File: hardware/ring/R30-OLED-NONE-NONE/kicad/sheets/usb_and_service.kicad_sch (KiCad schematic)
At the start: 4 parts, among them J1 USB4215-class 16P TH stakes

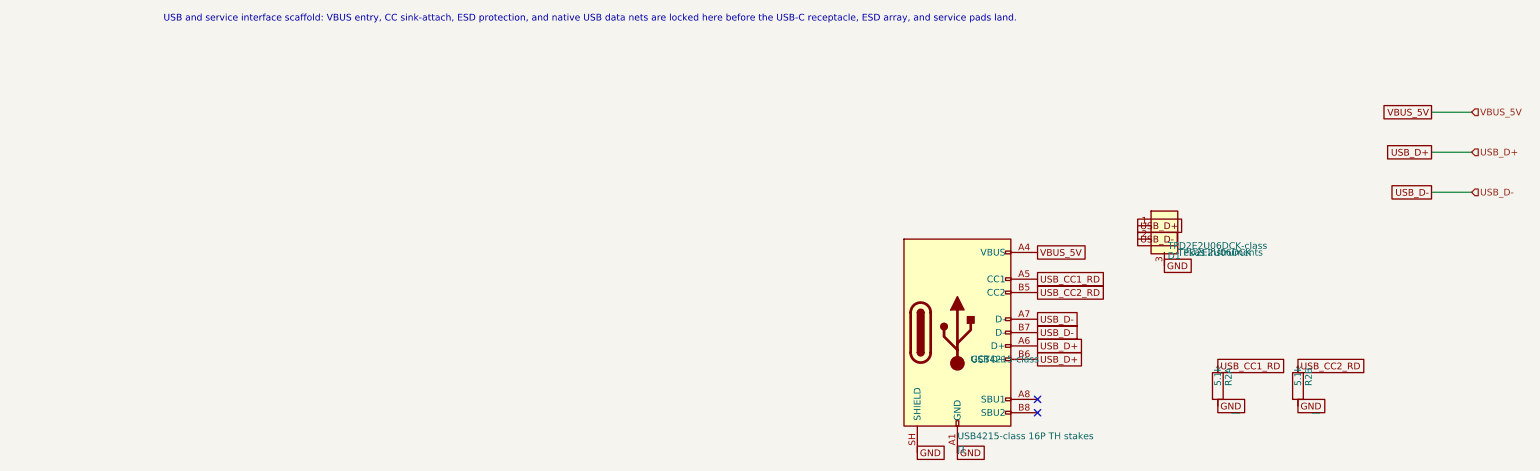
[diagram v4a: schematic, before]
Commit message: feat(r30): cut service hardware blockers
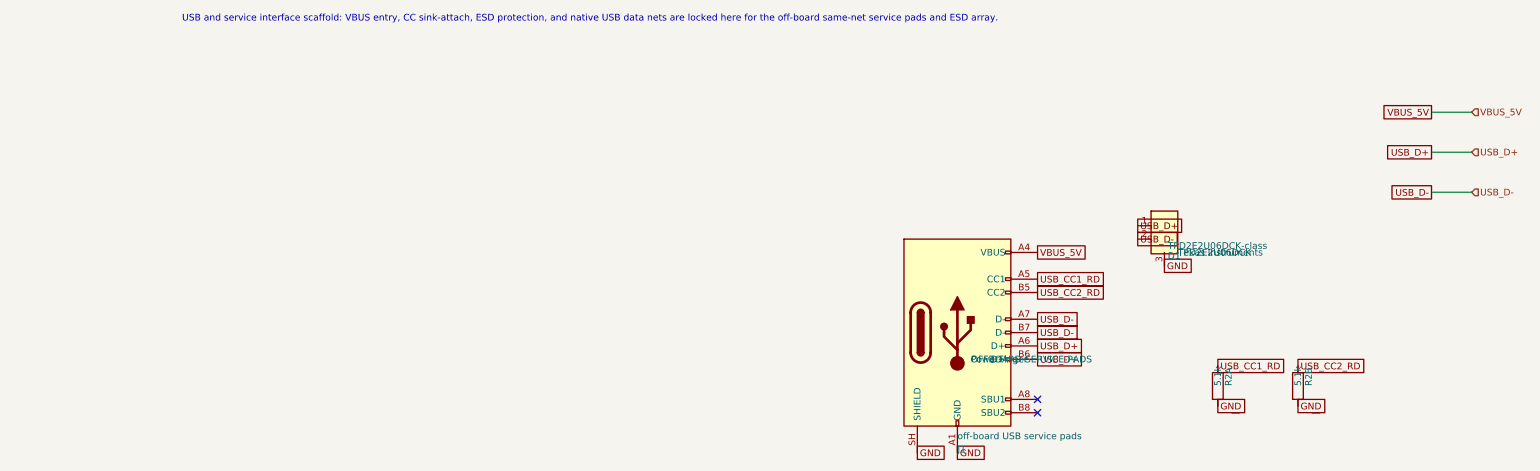
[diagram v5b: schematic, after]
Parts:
- J1: value USB4215-class 16P TH stakes -> off-board USB service pads; footprint PowerFinger_Ring:USB_C_Receptacle_GCT_USB4215_Class_16P_TH_Stakes -> PowerFinger_Ring:Offboard_USB_Service_SameNet; manufacturer GCT -> PowerFinger; mfg_part_num USB4215-class -> OFFBOARD-SERVICE-PADS
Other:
- note added: "USB and service interface scaffold: VBUS entry, CC sink-attach, ESD protection, and native USB data nets are locked here for the off-board same-net service pads and ESD array."
- note removed: "USB and service interface scaffold: VBUS entry, CC sink-attach, ESD protection, and native USB data nets are locked here before the USB-C receptacle, ESD array, and service pads land."
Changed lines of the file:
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@@
 			)
 		)
-		(property "Value" "USB4215-class 16P TH stakes"
+		(property "Value" "off-board USB service pads"
 			(at 90.17 99.695 0.0000)
 			(effects
@@
 			)
 		)
-		(property "Footprint" "PowerFinger_Ring:USB_C_Receptacle_GCT_USB4215_Class_16P_TH_Stakes"
+		(property "Footprint" "PowerFinger_Ring:Offboard_USB_Service_SameNet"
 			(at 93.98 80.01 0.0000)
 			(effects
@@
 			)
 		)
-		(property "mfg_part_num" "USB4215-class"
+		(property "mfg_part_num" "OFFBOARD-SERVICE-PADS"
 			(at 92.71 85.0899 0)
 			(effects
@@
 			)
 		)
-		(property "manufacturer" "GCT"
+		(property "manufacturer" "PowerFinger"
 			(at 92.71 85.0899 0)
 			(effects
@@
 		(at 105.41 95.25)
 	)
-	(text "USB and service interface scaffold: VBUS entry, CC sink-attach, ESD protection, and native USB data nets are locked here before the USB-C receptacle, ESD array, and service pads land."
+	(text "USB and service interface scaffold: VBUS entry, CC sink-attach, ESD protection, and native USB data nets are locked here for the off-board same-net service pads and ESD array."
 		(exclude_from_sim no)
 		(at 20.32 20.32 0.0000)
